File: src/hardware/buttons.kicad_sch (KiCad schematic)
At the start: 30 parts

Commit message: Changed footprints from 0603 to 0402
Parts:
- C18, C19, C20, C21, C22, C23, C24, C25, C26, C27: footprint Capacitor_SMD:C_0603_1608Metric -> Capacitor_SMD:C_0504_1310Metric
- R13, R14, R15, R16, R17, R18, R19, R20, R21, R22: footprint Resistor_SMD:R_0603_1608Metric -> Resistor_SMD:R_0402_1005Metric
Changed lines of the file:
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@@
 			)
 		)
-		(property "Footprint" "Resistor_SMD:R_0603_1608Metric"
+		(property "Footprint" "Resistor_SMD:R_0402_1005Metric"
 			(at 125.73 119.888 90)
 			(effects
@@
 			)
 		)
-		(property "Footprint" "Capacitor_SMD:C_0603_1608Metric"
+		(property "Footprint" "Capacitor_SMD:C_0504_1310Metric"
 			(at 131.1148 49.53 0)
 			(effects
@@
 			)
 		)
-		(property "Footprint" "Capacitor_SMD:C_0603_1608Metric"
+		(property "Footprint" "Capacitor_SMD:C_0504_1310Metric"
 			(at 131.1148 107.95 0)
 			(effects
@@
 			)
 		)
-		(property "Footprint" "Resistor_SMD:R_0603_1608Metric"
+		(property "Footprint" "Resistor_SMD:R_0402_1005Metric"
 			(at 171.45 100.838 90)
 			(effects
@@
 			)
 		)
-		(property "Footprint" "Resistor_SMD:R_0603_1608Metric"
+		(property "Footprint" "Resistor_SMD:R_0402_1005Metric"
 			(at 125.73 100.838 90)
 			(effects
@@
 			)
 		)
-		(property "Footprint" "Resistor_SMD:R_0603_1608Metric"
+		(property "Footprint" "Resistor_SMD:R_0402_1005Metric"
 			(at 171.45 81.788 90)
 			(effects
@@
 			)
 		)
-		(property "Footprint" "Capacitor_SMD:C_0603_1608Metric"
+		(property "Footprint" "Capacitor_SMD:C_0504_1310Metric"
 			(at 166.0652 88.9 0)
 			(effects
@@
 			)
 		)
-		(property "Footprint" "Capacitor_SMD:C_0603_1608Metric"
+		(property "Footprint" "Capacitor_SMD:C_0504_1310Metric"
 			(at 166.0652 69.85 0)
 			(effects
@@
 			)
 		)
-		(property "Footprint" "Resistor_SMD:R_0603_1608Metric"
+		(property "Footprint" "Resistor_SMD:R_0402_1005Metric"
 			(at 171.45 61.468 90)
 			(effects
@@
 			)
 		)
-		(property "Footprint" "Capacitor_SMD:C_0603_1608Metric"
+		(property "Footprint" "Capacitor_SMD:C_0504_1310Metric"
 			(at 131.1148 69.85 0)
 			(effects
@@
 			)
 		)
-		(property "Footprint" "Capacitor_SMD:C_0603_1608Metric"
+		(property "Footprint" "Capacitor_SMD:C_0504_1310Metric"
 			(at 166.0652 107.95 0)
 			(effects
@@
 			)
 		)
-		(property "Footprint" "Resistor_SMD:R_0603_1608Metric"
+		(property "Footprint" "Resistor_SMD:R_0402_1005Metric"
 			(at 125.73 138.938 90)
 			(effects
@@
 			)
 		)
-		(property "Footprint" "Capacitor_SMD:C_0603_1608Metric"
+		(property "Footprint" "Capacitor_SMD:C_0504_1310Metric"
 			(at 131.1148 88.9 0)
 			(effects
@@
 			)
 		)
-		(property "Footprint" "Resistor_SMD:R_0603_1608Metric"
+		(property "Footprint" "Resistor_SMD:R_0402_1005Metric"
 			(at 171.45 138.938 90)
 			(effects
@@
 			)
 		)
-		(property "Footprint" "Resistor_SMD:R_0603_1608Metric"
+		(property "Footprint" "Resistor_SMD:R_0402_1005Metric"
 			(at 171.45 119.888 90)
 			(effects
@@
 			)
 		)
-		(property "Footprint" "Capacitor_SMD:C_0603_1608Metric"
+		(property "Footprint" "Capacitor_SMD:C_0504_1310Metric"
 			(at 166.0652 49.53 0)
 			(effects
@@
 			)
 		)
-		(property "Footprint" "Resistor_SMD:R_0603_1608Metric"
+		(property "Footprint" "Resistor_SMD:R_0402_1005Metric"
 			(at 125.73 61.468 90)
 			(effects
@@
 			)
 		)
-		(property "Footprint" "Resistor_SMD:R_0603_1608Metric"
+		(property "Footprint" "Resistor_SMD:R_0402_1005Metric"
 			(at 125.73 81.788 90)
 			(effects
@@
 			)
 		)
-		(property "Footprint" "Capacitor_SMD:C_0603_1608Metric"
+		(property "Footprint" "Capacitor_SMD:C_0504_1310Metric"
 			(at 166.0652 127 0)
 			(effects
@@
 			)
 		)
-		(property "Footprint" "Capacitor_SMD:C_0603_1608Metric"
+		(property "Footprint" "Capacitor_SMD:C_0504_1310Metric"
 			(at 131.1148 127 0)
 			(effects

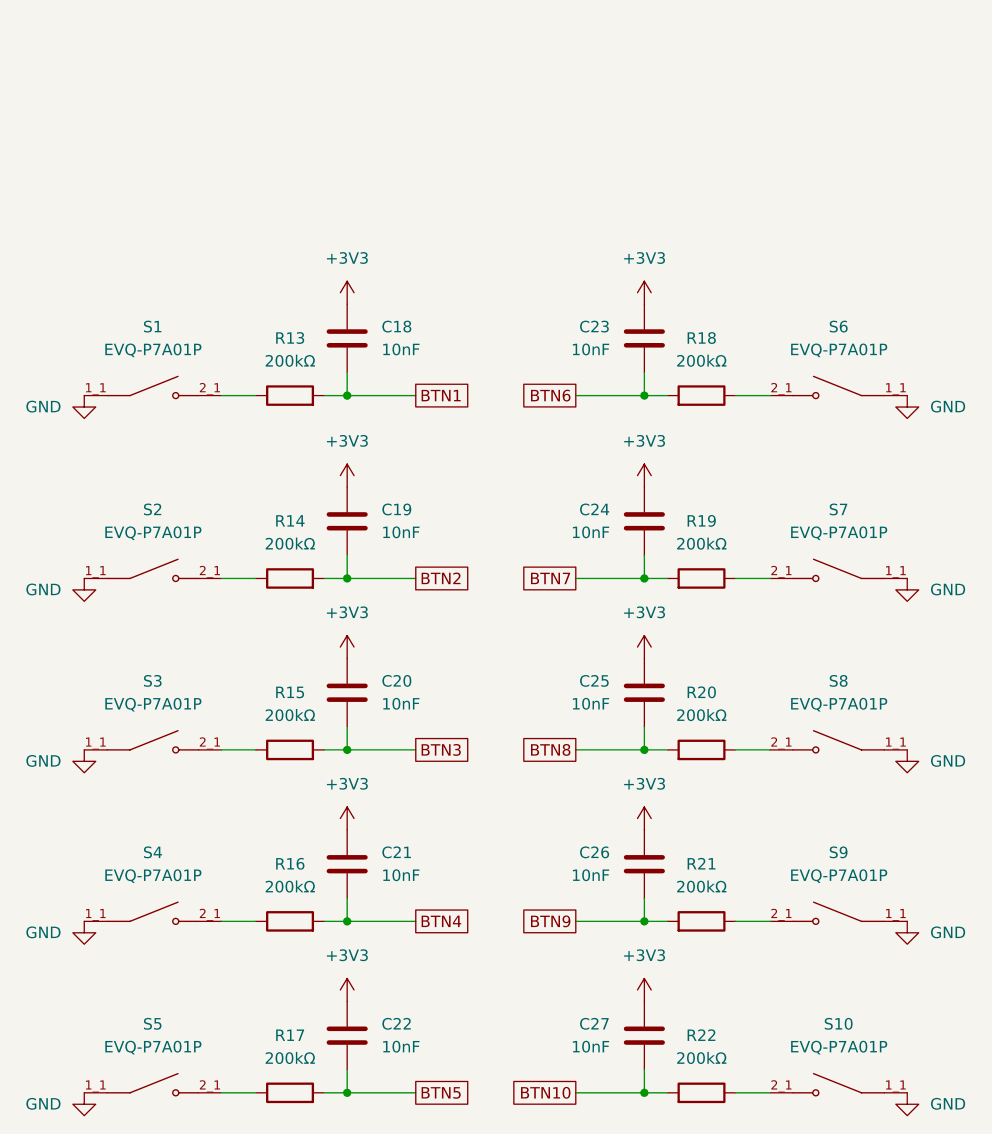
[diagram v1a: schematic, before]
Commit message: Replaced global labels with pin headers
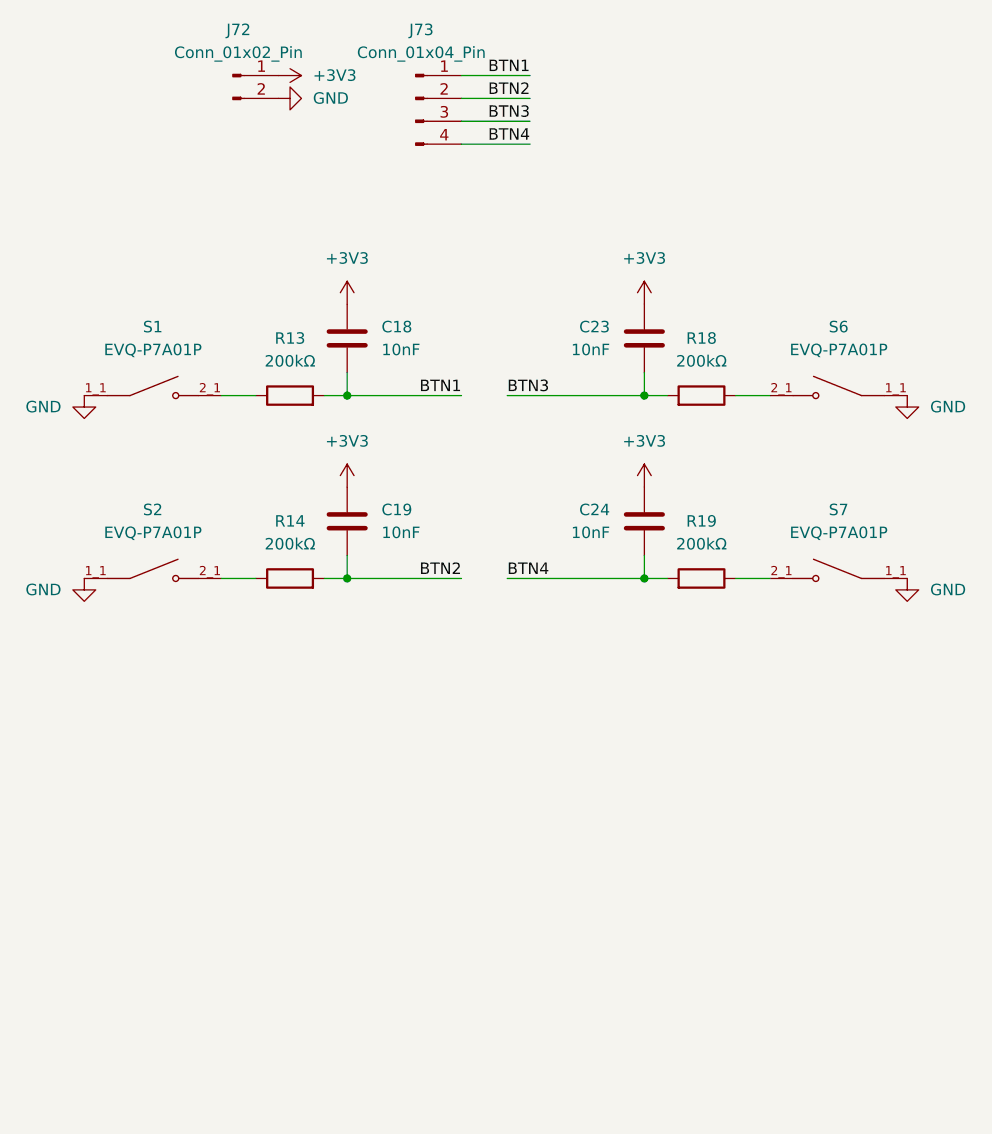
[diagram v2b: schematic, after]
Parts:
- removed C20, C21, C22, C25, C26, C27: 10nF, Capacitor_SMD:C_0504_1310Metric, symbol Device:C
- removed R15, R16, R17, R20, R21, R22: 200kΩ, Resistor_SMD:R_0402_1005Metric, symbol Device:R
- removed S10, S3, S4, S5, S8, S9: EVQ-P7A01P, Project:SW_EVQ-P7A01P, symbol EVQ-P7A01P:EVQ-P7A01P
- added J72: Conn_01x02_Pin, symbol Connector:Conn_01x02_Pin
- added J73: Conn_01x04_Pin, symbol Connector:Conn_01x04_Pin
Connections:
- net BTN6 is gone; now on net BTN3: C23.1, R18.2
- net BTN7 is gone; now on net BTN4: C24.1, R19.2
- net +3V3: now also J72.1 (Pin_1)
- net BTN1: now also J73.1 (Pin_1)
- net BTN2: now also J73.2 (Pin_2)
- net BTN3: now also J73.3 (Pin_3)
- net BTN4: now also J73.4 (Pin_4)
- net GND: now also J72.2 (Pin_2)

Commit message: Reannotated schematic
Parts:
- renumbered C23 to C20, C24 to C21, J72 to J22, J73 to J23, R18 to R15, R19 to R16, S6 to S3, S7 to S4
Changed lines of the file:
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@@
 		(dnp no)
 		(fields_autoplaced yes)
-		(property "Reference" "#PWR055"
+		(property "Reference" "#PWR067"
 			(at 194.31 66.04 0)
 			(effects
@@
 			(project "raywatch"
 				(path "/7b654ee8-2a53-4d39-8b7d-32c7bb3cb0ed/dd50c693-c2d1-4da4-86ca-2eae732704f9"
-					(reference "#PWR055")
+					(reference "#PWR067")
 					(unit 1)
 				)
@@
 		(dnp no)
 		(fields_autoplaced yes)
-		(property "Reference" "#PWR051"
+		(property "Reference" "#PWR059"
 			(at 102.87 66.04 0)
 			(effects
@@
 			(project "raywatch"
 				(path "/7b654ee8-2a53-4d39-8b7d-32c7bb3cb0ed/dd50c693-c2d1-4da4-86ca-2eae732704f9"
-					(reference "#PWR051")
+					(reference "#PWR059")
 					(unit 1)
 				)
@@
 		(dnp no)
 		(fields_autoplaced yes)
-		(property "Reference" "#PWR056"
+		(property "Reference" "#PWR068"
 			(at 194.31 86.36 0)
 			(effects
@@
 			(project "raywatch"
 				(path "/7b654ee8-2a53-4d39-8b7d-32c7bb3cb0ed/dd50c693-c2d1-4da4-86ca-2eae732704f9"
-					(reference "#PWR056")
+					(reference "#PWR068")
 					(unit 1)
 				)
@@
 		(dnp no)
 		(fields_autoplaced yes)
-		(property "Reference" "R19"
+		(property "Reference" "R16"
 			(at 171.45 73.66 90)
 			(effects
@@
 			(project "raywatch"
 				(path "/7b654ee8-2a53-4d39-8b7d-32c7bb3cb0ed/dd50c693-c2d1-4da4-86ca-2eae732704f9"
-					(reference "R19")
+					(reference "R16")
 					(unit 1)
 				)
@@
 		(dnp no)
 		(fields_autoplaced yes)
-		(property "Reference" "C24"
+		(property "Reference" "C21"
 			(at 161.29 72.3899 0)
 			(effects
@@
 			(project "raywatch"
 				(path "/7b654ee8-2a53-4d39-8b7d-32c7bb3cb0ed/dd50c693-c2d1-4da4-86ca-2eae732704f9"
-					(reference "C24")
+					(reference "C21")
 					(unit 1)
 				)
@@
 		(dnp no)
 		(fields_autoplaced yes)
-		(property "Reference" "R18"
+		(property "Reference" "R15"
 			(at 171.45 53.34 90)
 			(effects
@@
 			(project "raywatch"
 				(path "/7b654ee8-2a53-4d39-8b7d-32c7bb3cb0ed/dd50c693-c2d1-4da4-86ca-2eae732704f9"
-					(reference "R18")
+					(reference "R15")
 					(unit 1)
 				)
@@
 		(dnp no)
 		(fields_autoplaced yes)
-		(property "Reference" "J73"
+		(property "Reference" "J23"
 			(at 140.335 19.05 0)
 			(effects
@@
 			(project "raywatch"
 				(path "/7b654ee8-2a53-4d39-8b7d-32c7bb3cb0ed/dd50c693-c2d1-4da4-86ca-2eae732704f9"
-					(reference "J73")
+					(reference "J23")
 					(unit 1)
 				)
@@
 		(dnp no)
 		(fields_autoplaced yes)
-		(property "Reference" "#PWR053"
+		(property "Reference" "#PWR062"
 			(at 130.81 26.67 0)
 			(effects
@@
 			(project "raywatch"
 				(path "/7b654ee8-2a53-4d39-8b7d-32c7bb3cb0ed/dd50c693-c2d1-4da4-86ca-2eae732704f9"
-					(reference "#PWR053")
+					(reference "#PWR062")
 					(unit 1)
 				)
@@
 		(dnp no)
 		(fields_autoplaced yes)
-		(property "Reference" "#PWR050"
+		(property "Reference" "#PWR060"
 			(at 102.87 86.36 0)
 			(effects
@@
 			(project "raywatch"
 				(path "/7b654ee8-2a53-4d39-8b7d-32c7bb3cb0ed/dd50c693-c2d1-4da4-86ca-2eae732704f9"
-					(reference "#PWR050")
+					(reference "#PWR060")
 					(unit 1)
 				)
@@
 		(dnp no)
 		(fields_autoplaced yes)
-		(property "Reference" "C23"
+		(property "Reference" "C20"
 			(at 161.29 52.0699 0)
 			(effects
@@
 			(project "raywatch"
 				(path "/7b654ee8-2a53-4d39-8b7d-32c7bb3cb0ed/dd50c693-c2d1-4da4-86ca-2eae732704f9"
-					(reference "C23")
+					(reference "C20")
 					(unit 1)
 				)
@@
 		(dnp no)
 		(fields_autoplaced yes)
-		(property "Reference" "J72"
+		(property "Reference" "J22"
 			(at 120.015 19.05 0)
 			(effects
@@
 			(project "raywatch"
 				(path "/7b654ee8-2a53-4d39-8b7d-32c7bb3cb0ed/dd50c693-c2d1-4da4-86ca-2eae732704f9"
-					(reference "J72")
+					(reference "J22")
 					(unit 1)
 				)
@@
 		(dnp no)
 		(fields_autoplaced yes)
-		(property "Reference" "#PWR052"
+		(property "Reference" "#PWR061"
 			(at 120.65 24.13 0)
 			(effects
@@
 			(project "raywatch"
 				(path "/7b654ee8-2a53-4d39-8b7d-32c7bb3cb0ed/dd50c693-c2d1-4da4-86ca-2eae732704f9"
-					(reference "#PWR052")
+					(reference "#PWR061")
 					(unit 1)
 				)
@@
 		(dnp no)
 		(fields_autoplaced yes)
-		(property "Reference" "#PWR061"
+		(property "Reference" "#PWR064"
 			(at 132.08 73.66 0)
 			(effects
@@
 			(project "raywatch"
 				(path "/7b654ee8-2a53-4d39-8b7d-32c7bb3cb0ed/dd50c693-c2d1-4da4-86ca-2eae732704f9"
-					(reference "#PWR061")
+					(reference "#PWR064")
 					(unit 1)
 				)
@@
 		(dnp no)
 		(fields_autoplaced yes)
-		(property "Reference" "#PWR060"
+		(property "Reference" "#PWR063"
 			(at 132.08 53.34 0)
 			(effects
@@
 			(project "raywatch"
 				(path "/7b654ee8-2a53-4d39-8b7d-32c7bb3cb0ed/dd50c693-c2d1-4da4-86ca-2eae732704f9"
-					(reference "#PWR060")
+					(reference "#PWR063")
 					(unit 1)
 				)
@@
 		(dnp no)
 		(fields_autoplaced yes)
-		(property "Reference" "S7"
+		(property "Reference" "S4"
 			(at 186.69 72.39 0)
 			(effects
@@
 			(project "raywatch"
 				(path "/7b654ee8-2a53-4d39-8b7d-32c7bb3cb0ed/dd50c693-c2d1-4da4-86ca-2eae732704f9"
-					(reference "S7")
+					(reference "S4")
 					(unit 1)
 				)
@@
 		(dnp no)
 		(fields_autoplaced yes)
-		(property "Reference" "S6"
+		(property "Reference" "S3"
 			(at 186.69 52.07 0)
 			(effects
@@
 			(project "raywatch"
 				(path "/7b654ee8-2a53-4d39-8b7d-32c7bb3cb0ed/dd50c693-c2d1-4da4-86ca-2eae732704f9"
-					(reference "S6")
-					(unit 1)
-				)
+					(reference "S3")
+					(unit 1)
+				)

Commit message: Assigned pin header footprints
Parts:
- J22: footprint (none) -> Connector_PinHeader_2.54mm:PinHeader_1x02_P2.54mm_Horizontal
- J23: footprint (none) -> Connector_PinHeader_2.54mm:PinHeader_1x04_P2.54mm_Horizontal
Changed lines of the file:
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@@
 			)
 		)
-		(property "Footprint" ""
+		(property "Footprint" "Connector_PinHeader_2.54mm:PinHeader_1x04_P2.54mm_Horizontal"
 			(at 139.7 26.67 0)
 			(effects
@@
 			)
 		)
-		(property "Footprint" ""
+		(property "Footprint" "Connector_PinHeader_2.54mm:PinHeader_1x02_P2.54mm_Horizontal"
 			(at 119.38 24.13 0)
 			(effects

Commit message: Changed pin headers to vertical
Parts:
- J22: footprint Connector_PinHeader_2.54mm:PinHeader_1x02_P2.54mm_Horizontal -> Connector_PinHeader_2.54mm:PinHeader_1x02_P2.54mm_Vertical
- J23: footprint Connector_PinHeader_2.54mm:PinHeader_1x04_P2.54mm_Horizontal -> Connector_PinHeader_2.54mm:PinHeader_1x04_P2.54mm_Vertical
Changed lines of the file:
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@@
 			)
 		)
-		(property "Footprint" "Connector_PinHeader_2.54mm:PinHeader_1x04_P2.54mm_Horizontal"
+		(property "Footprint" "Connector_PinHeader_2.54mm:PinHeader_1x04_P2.54mm_Vertical"
 			(at 139.7 26.67 0)
 			(effects
@@
 			)
 		)
-		(property "Footprint" "Connector_PinHeader_2.54mm:PinHeader_1x02_P2.54mm_Horizontal"
+		(property "Footprint" "Connector_PinHeader_2.54mm:PinHeader_1x02_P2.54mm_Vertical"
 			(at 119.38 24.13 0)
 			(effects

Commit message: Fixed connector footprints; Changed conectors from 2.54 to 1.27
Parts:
- J22: footprint Connector_PinHeader_2.54mm:PinHeader_1x02_P2.54mm_Vertical -> Connector_PinHeader_1.27mm:PinHeader_1x02_P1.27mm_Vertical
- J23: footprint Connector_PinHeader_2.54mm:PinHeader_1x04_P2.54mm_Vertical -> Connector_PinHeader_1.27mm:PinHeader_1x04_P1.27mm_Vertical
- renumbered R13 to R14, R14 to R15, R15 to R16, R16 to R17
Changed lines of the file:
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@@
 		(dnp no)
 		(fields_autoplaced yes)
-		(property "Reference" "#PWR067"
+		(property "Reference" "#PWR069"
 			(at 194.31 66.04 0)
 			(effects
@@
 			(project "raywatch"
 				(path "/7b654ee8-2a53-4d39-8b7d-32c7bb3cb0ed/dd50c693-c2d1-4da4-86ca-2eae732704f9"
-					(reference "#PWR067")
+					(reference "#PWR069")
 					(unit 1)
 				)
@@
 		(dnp no)
 		(fields_autoplaced yes)
-		(property "Reference" "#PWR059"
+		(property "Reference" "#PWR061"
 			(at 102.87 66.04 0)
 			(effects
@@
 			(project "raywatch"
 				(path "/7b654ee8-2a53-4d39-8b7d-32c7bb3cb0ed/dd50c693-c2d1-4da4-86ca-2eae732704f9"
-					(reference "#PWR059")
+					(reference "#PWR061")
 					(unit 1)
 				)
@@
 		(dnp no)
 		(fields_autoplaced yes)
-		(property "Reference" "#PWR068"
+		(property "Reference" "#PWR070"
 			(at 194.31 86.36 0)
 			(effects
@@
 			(project "raywatch"
 				(path "/7b654ee8-2a53-4d39-8b7d-32c7bb3cb0ed/dd50c693-c2d1-4da4-86ca-2eae732704f9"
-					(reference "#PWR068")
+					(reference "#PWR070")
 					(unit 1)
 				)
@@
 		(dnp no)
 		(fields_autoplaced yes)
-		(property "Reference" "R16"
+		(property "Reference" "R17"
 			(at 171.45 73.66 90)
 			(effects
@@
 			(project "raywatch"
 				(path "/7b654ee8-2a53-4d39-8b7d-32c7bb3cb0ed/dd50c693-c2d1-4da4-86ca-2eae732704f9"
-					(reference "R16")
+					(reference "R17")
 					(unit 1)
 				)
@@
 		(dnp no)
 		(fields_autoplaced yes)
-		(property "Reference" "#PWR065"
+		(property "Reference" "#PWR067"
 			(at 165.1 53.34 0)
 			(effects
@@
 			(project "raywatch"
 				(path "/7b654ee8-2a53-4d39-8b7d-32c7bb3cb0ed/dd50c693-c2d1-4da4-86ca-2eae732704f9"
-					(reference "#PWR065")
+					(reference "#PWR067")
 					(unit 1)
 				)
@@
 		(dnp no)
 		(fields_autoplaced yes)
-		(property "Reference" "R15"
+		(property "Reference" "R16"
 			(at 171.45 53.34 90)
 			(effects
@@
 			(project "raywatch"
 				(path "/7b654ee8-2a53-4d39-8b7d-32c7bb3cb0ed/dd50c693-c2d1-4da4-86ca-2eae732704f9"
-					(reference "R15")
+					(reference "R16")
 					(unit 1)
 				)
@@
 			)
 		)
-		(property "Footprint" "Connector_PinHeader_2.54mm:PinHeader_1x04_P2.54mm_Vertical"
+		(property "Footprint" "Connector_PinHeader_1.27mm:PinHeader_1x04_P1.27mm_Vertical"
 			(at 139.7 26.67 0)
 			(effects
@@
 		(dnp no)
 		(fields_autoplaced yes)
-		(property "Reference" "#PWR062"
+		(property "Reference" "#PWR064"
 			(at 130.81 26.67 0)
 			(effects
@@
 			(project "raywatch"
 				(path "/7b654ee8-2a53-4d39-8b7d-32c7bb3cb0ed/dd50c693-c2d1-4da4-86ca-2eae732704f9"
-					(reference "#PWR062")
+					(reference "#PWR064")
 					(unit 1)
 				)
@@
 		(dnp no)
 		(fields_autoplaced yes)
-		(property "Reference" "#PWR060"
+		(property "Reference" "#PWR062"
 			(at 102.87 86.36 0)
 			(effects
@@
 			(project "raywatch"
 				(path "/7b654ee8-2a53-4d39-8b7d-32c7bb3cb0ed/dd50c693-c2d1-4da4-86ca-2eae732704f9"
-					(reference "#PWR060")
+					(reference "#PWR062")
 					(unit 1)
 				)
@@
 		(dnp no)
 		(fields_autoplaced yes)
-		(property "Reference" "R13"
+		(property "Reference" "R14"
 			(at 125.73 53.34 90)
 			(effects
@@
 			(project "raywatch"
 				(path "/7b654ee8-2a53-4d39-8b7d-32c7bb3cb0ed/dd50c693-c2d1-4da4-86ca-2eae732704f9"
-					(reference "R13")
+					(reference "R14")
 					(unit 1)
 				)
@@
 			)
 		)
-		(property "Footprint" "Connector_PinHeader_2.54mm:PinHeader_1x02_P2.54mm_Vertical"
+		(property "Footprint" "Connector_PinHeader_1.27mm:PinHeader_1x02_P1.27mm_Vertical"
 			(at 119.38 24.13 0)
 			(effects
@@
 		(dnp no)
 		(fields_autoplaced yes)
-		(property "Reference" "#PWR061"
+		(property "Reference" "#PWR063"
 			(at 120.65 24.13 0)
 			(effects
@@
 			(project "raywatch"
 				(path "/7b654ee8-2a53-4d39-8b7d-32c7bb3cb0ed/dd50c693-c2d1-4da4-86ca-2eae732704f9"
-					(reference "#PWR061")
+					(reference "#PWR063")
 					(unit 1)
 				)
@@
 		(dnp no)
 		(fields_autoplaced yes)
-		(property "Reference" "#PWR064"
+		(property "Reference" "#PWR066"
 			(at 132.08 73.66 0)
 			(effects
@@
 			(project "raywatch"
 				(path "/7b654ee8-2a53-4d39-8b7d-32c7bb3cb0ed/dd50c693-c2d1-4da4-86ca-2eae732704f9"
-					(reference "#PWR064")
+					(reference "#PWR066")
 					(unit 1)
 				)
@@
 		(dnp no)
 		(fields_autoplaced yes)
-		(property "Reference" "#PWR066"
+		(property "Reference" "#PWR068"
 			(at 165.1 73.66 0)
 			(effects
@@
 			(project "raywatch"
 				(path "/7b654ee8-2a53-4d39-8b7d-32c7bb3cb0ed/dd50c693-c2d1-4da4-86ca-2eae732704f9"
-					(reference "#PWR066")
+					(reference "#PWR068")
 					(unit 1)
 				)
@@
 		(dnp no)
 		(fields_autoplaced yes)
-		(property "Reference" "R14"
+		(property "Reference" "R15"
 			(at 125.73 73.66 90)
 			(effects
@@
 			(project "raywatch"
 				(path "/7b654ee8-2a53-4d39-8b7d-32c7bb3cb0ed/dd50c693-c2d1-4da4-86ca-2eae732704f9"
-					(reference "R14")
+					(reference "R15")
 					(unit 1)
 				)
@@
 		(dnp no)
 		(fields_autoplaced yes)
-		(property "Reference" "#PWR063"
+		(property "Reference" "#PWR065"
 			(at 132.08 53.34 0)
 			(effects
@@
 			(project "raywatch"
 				(path "/7b654ee8-2a53-4d39-8b7d-32c7bb3cb0ed/dd50c693-c2d1-4da4-86ca-2eae732704f9"
-					(reference "#PWR063")
-					(unit 1)
-				)
+					(reference "#PWR065")
+					(unit 1)
+				)

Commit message: Fixes; Added TPM PCB
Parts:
- C18, C19, C20, C21: footprint Capacitor_SMD:C_0504_1310Metric -> Capacitor_SMD:C_0402_1005Metric
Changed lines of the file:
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@@
 			)
 		)
-		(property "Footprint" "Capacitor_SMD:C_0504_1310Metric"
+		(property "Footprint" "Capacitor_SMD:C_0402_1005Metric"
 			(at 131.1148 49.53 0)
 			(effects
@@
 			)
 		)
-		(property "Footprint" "Capacitor_SMD:C_0504_1310Metric"
+		(property "Footprint" "Capacitor_SMD:C_0402_1005Metric"
 			(at 166.0652 69.85 0)
 			(effects
@@
 			)
 		)
-		(property "Footprint" "Capacitor_SMD:C_0504_1310Metric"
+		(property "Footprint" "Capacitor_SMD:C_0402_1005Metric"
 			(at 131.1148 69.85 0)
 			(effects
@@
 			)
 		)
-		(property "Footprint" "Capacitor_SMD:C_0504_1310Metric"
+		(property "Footprint" "Capacitor_SMD:C_0402_1005Metric"
 			(at 166.0652 49.53 0)
 			(effects
